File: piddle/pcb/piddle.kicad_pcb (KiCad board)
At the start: 2 copper layers, 133.5 x 118 mm, 68 parts, among them J1 Conn_01x03_Socket, J10 Conn_01x03_Socket, J11 Conn_01x02_Socket, J12 Conn_01x02_Socket, J13 Conn_01x02_Pin, J2 Conn_01x03_Socket, J3 Conn_01x03_Socket, J4 Conn_01x03_Socket, J5 Conn_01x03_Socket, J7 Conn_01x03_Socket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

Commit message: Start 15 pin
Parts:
- removed D10, D14, D16, D18, D2, D20, D4, D6, D8: 1N4148, Diode_THT:D_DO-35_SOD27_P10.16mm_Horizontal
- moved D12 14.6 mm to (87.5, 143.6), turned to 0 degrees
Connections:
- D1 pad 1: Net-(D1-VDD) -> /4.3V
- D11 pad 1: Net-(D11-VDD) -> /4.3V
- D12 pad 1: Net-(D11-VDD) -> /4.3V
- D13 pad 1: Net-(D13-VDD) -> /4.3V
- D15 pad 1: Net-(D15-VDD) -> /4.3V
- D17 pad 1: Net-(D17-VDD) -> /4.3V
- D19 pad 1: Net-(D19-VDD) -> /4.3V
- D3 pad 1: Net-(D3-VDD) -> /4.3V
- D5 pad 1: Net-(D5-VDD) -> /4.3V
- D7 pad 1: Net-(D7-VDD) -> /4.3V
- D9 pad 1: Net-(D10-K) -> /4.3V
- J7 pad 2: Net-(D13-DOUT) -> Net-(D13-DIN)
- R7 pad 1: Net-(D13-DIN) -> Net-(D13-DOUT)
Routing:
- net +5V: track 282.5 -> 72.3 mm
- net +3.3V: track 42.2 -> 14.5 mm
- net Net-(D13-VDD): track 15.2 -> 0.00 mm
- net Net-(D10-K): track 14.2 -> 0.00 mm
- net Net-(D5-VDD): track 11.5 -> 0.00 mm
- net Net-(D17-VDD): track 11.3 -> 0.00 mm
- net Net-(D19-VDD): track 11.2 -> 0.00 mm
- net Net-(D1-VDD): track 11.0 -> 0.00 mm
- net Net-(D15-VDD): track 10.4 -> 0.00 mm
- net Net-(D11-VDD): track 10.0 -> 0.00 mm
- net Net-(D7-VDD): track 9.78 -> 0.00 mm
- net Net-(D3-VDD): track 9.72 -> 0.00 mm
- net /4.3V: track 0.00 -> 1.70 mm
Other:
- board size 133.5 x 118 mm -> 198.9 x 197.8 mm

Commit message: Add mounting holes
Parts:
- added REF**: MountingHole_3.2mm_M3, MountingHole:MountingHole_3.2mm_M3, F.Cu at (74.2, 163.8)
- added REF**: MountingHole_3.2mm_M3, MountingHole:MountingHole_3.2mm_M3, F.Cu at (64.5, 71.6)
- added REF**: MountingHole_3.2mm_M3, MountingHole:MountingHole_3.2mm_M3, F.Cu at (102.5, 188.3)
- added REF**: MountingHole_3.2mm_M3, MountingHole:MountingHole_3.2mm_M3, F.Cu at (189.7, 188.3)
- added REF**: MountingHole_3.2mm_M3, MountingHole:MountingHole_3.2mm_M3, F.Cu at (229.0, 144.8)
- added REF**: MountingHole_3.2mm_M3, MountingHole:MountingHole_3.2mm_M3, F.Cu at (233.8, 129.8)
- added REF**: MountingHole_3.2mm_M3, MountingHole:MountingHole_3.2mm_M3, F.Cu at (227.7, 71.6)
- added REF**: MountingHole_3.2mm_M3, MountingHole:MountingHole_3.2mm_M3, F.Cu at (57.8, 92.4)
- added REF**: MountingHole_3.2mm_M3, MountingHole:MountingHole_3.2mm_M3, F.Cu at (138.3, 199.3)
- added REF**: MountingHole_3.2mm_M3, MountingHole:MountingHole_3.2mm_M3, F.Cu at (234.5, 92.4)
- moved REF** 180.1 mm to (219.8, 58.0)
- moved REF** 168.0 mm to (205.2, 41.7)
- moved REF** 164.9 mm to (192.5, 32.5)
- moved REF** 123.5 mm to (207.5, 175.4)
- moved REF** 121.4 mm to (218.0, 163.8)
- moved REF** 113.3 mm to (236.1, 108.0)
- moved REF** 108.0 mm to (87.1, 41.7)
- moved REF** 106.3 mm to (84.7, 175.4)
- moved REF** 98.7 mm to (119.8, 23.5)
- moved REF** 98.1 mm to (56.1, 108.0)
- moved REF** 92.0 mm to (63.3, 144.8)
- moved REF** 90.4 mm to (58.4, 129.8)
- moved REF** 88.1 mm to (172.4, 23.5)
- moved REF** 84.7 mm to (135.1, 20.3)
- moved REF** 70.7 mm to (154.0, 199.3)
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
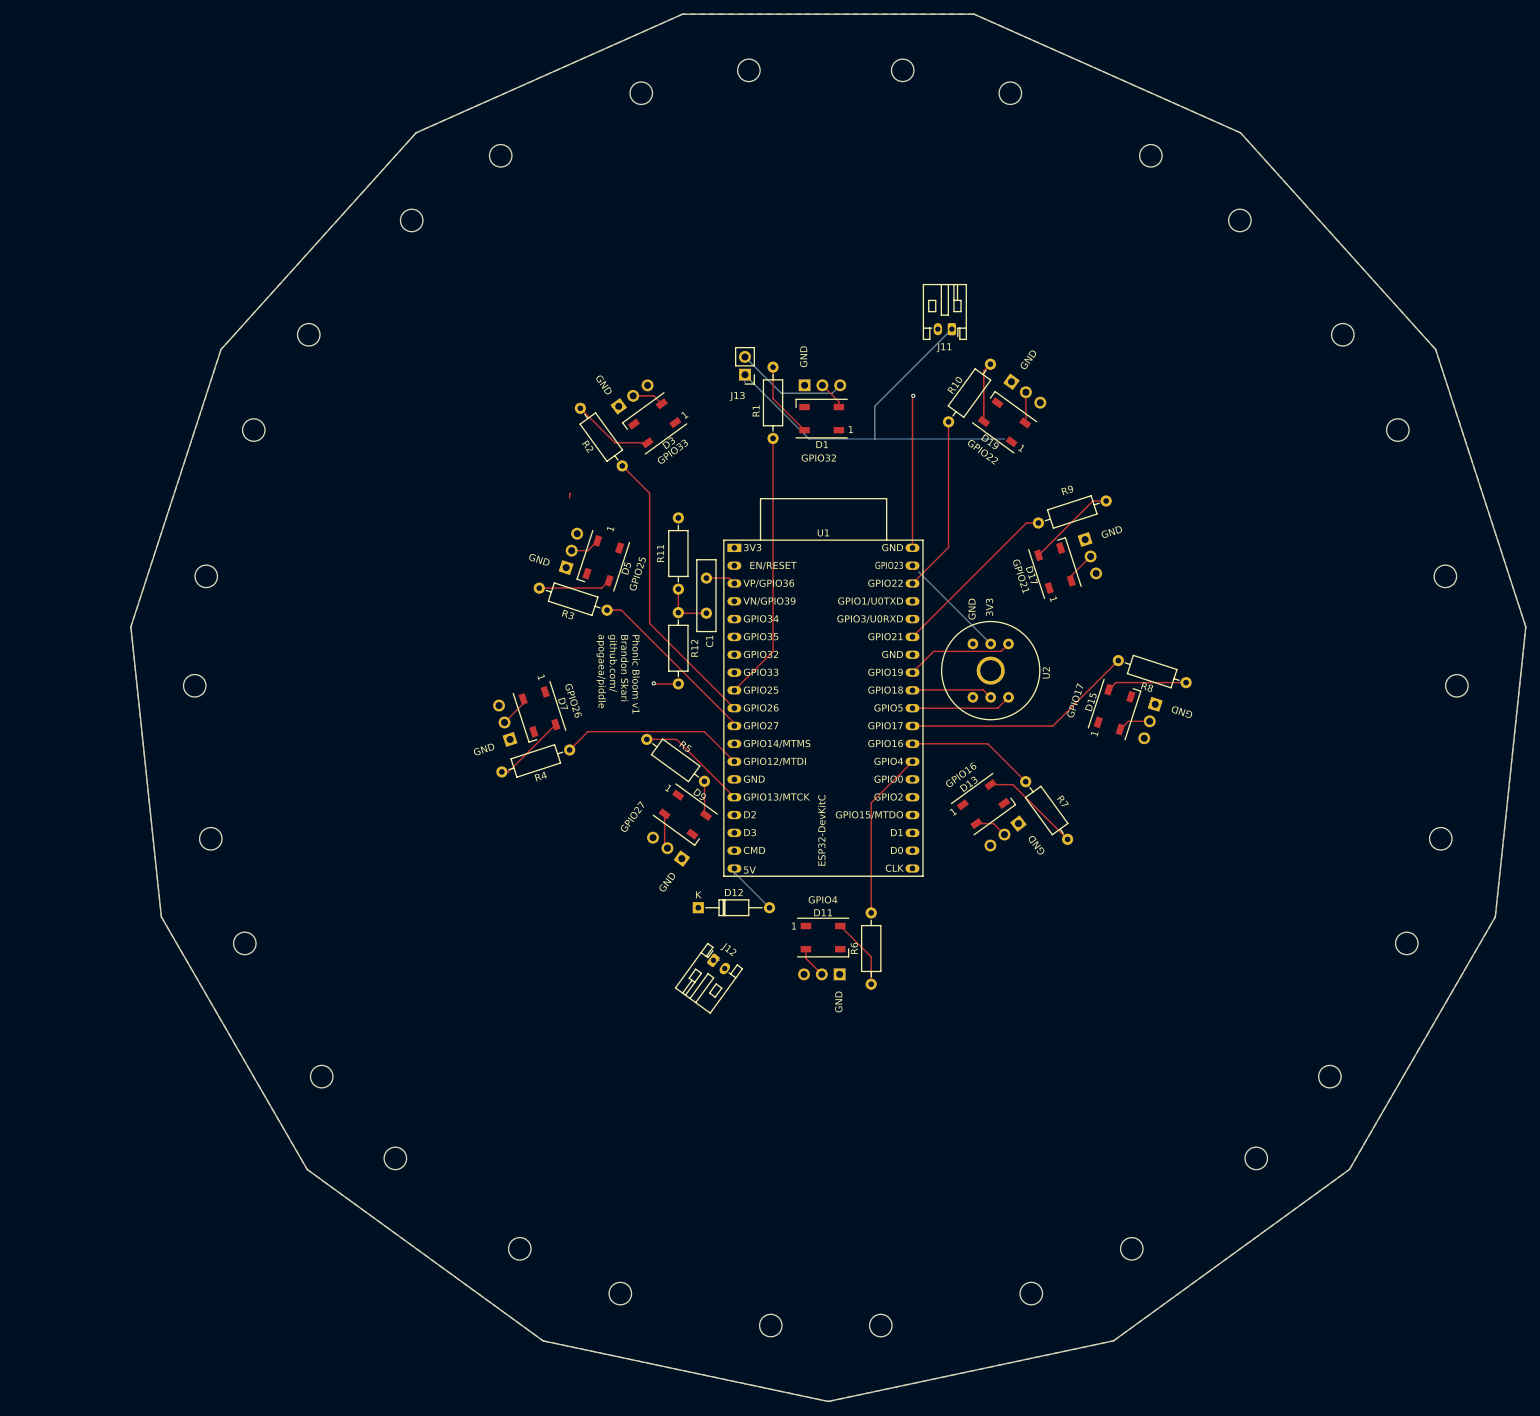
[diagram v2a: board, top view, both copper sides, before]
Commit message: Arrange components for 15-strip board
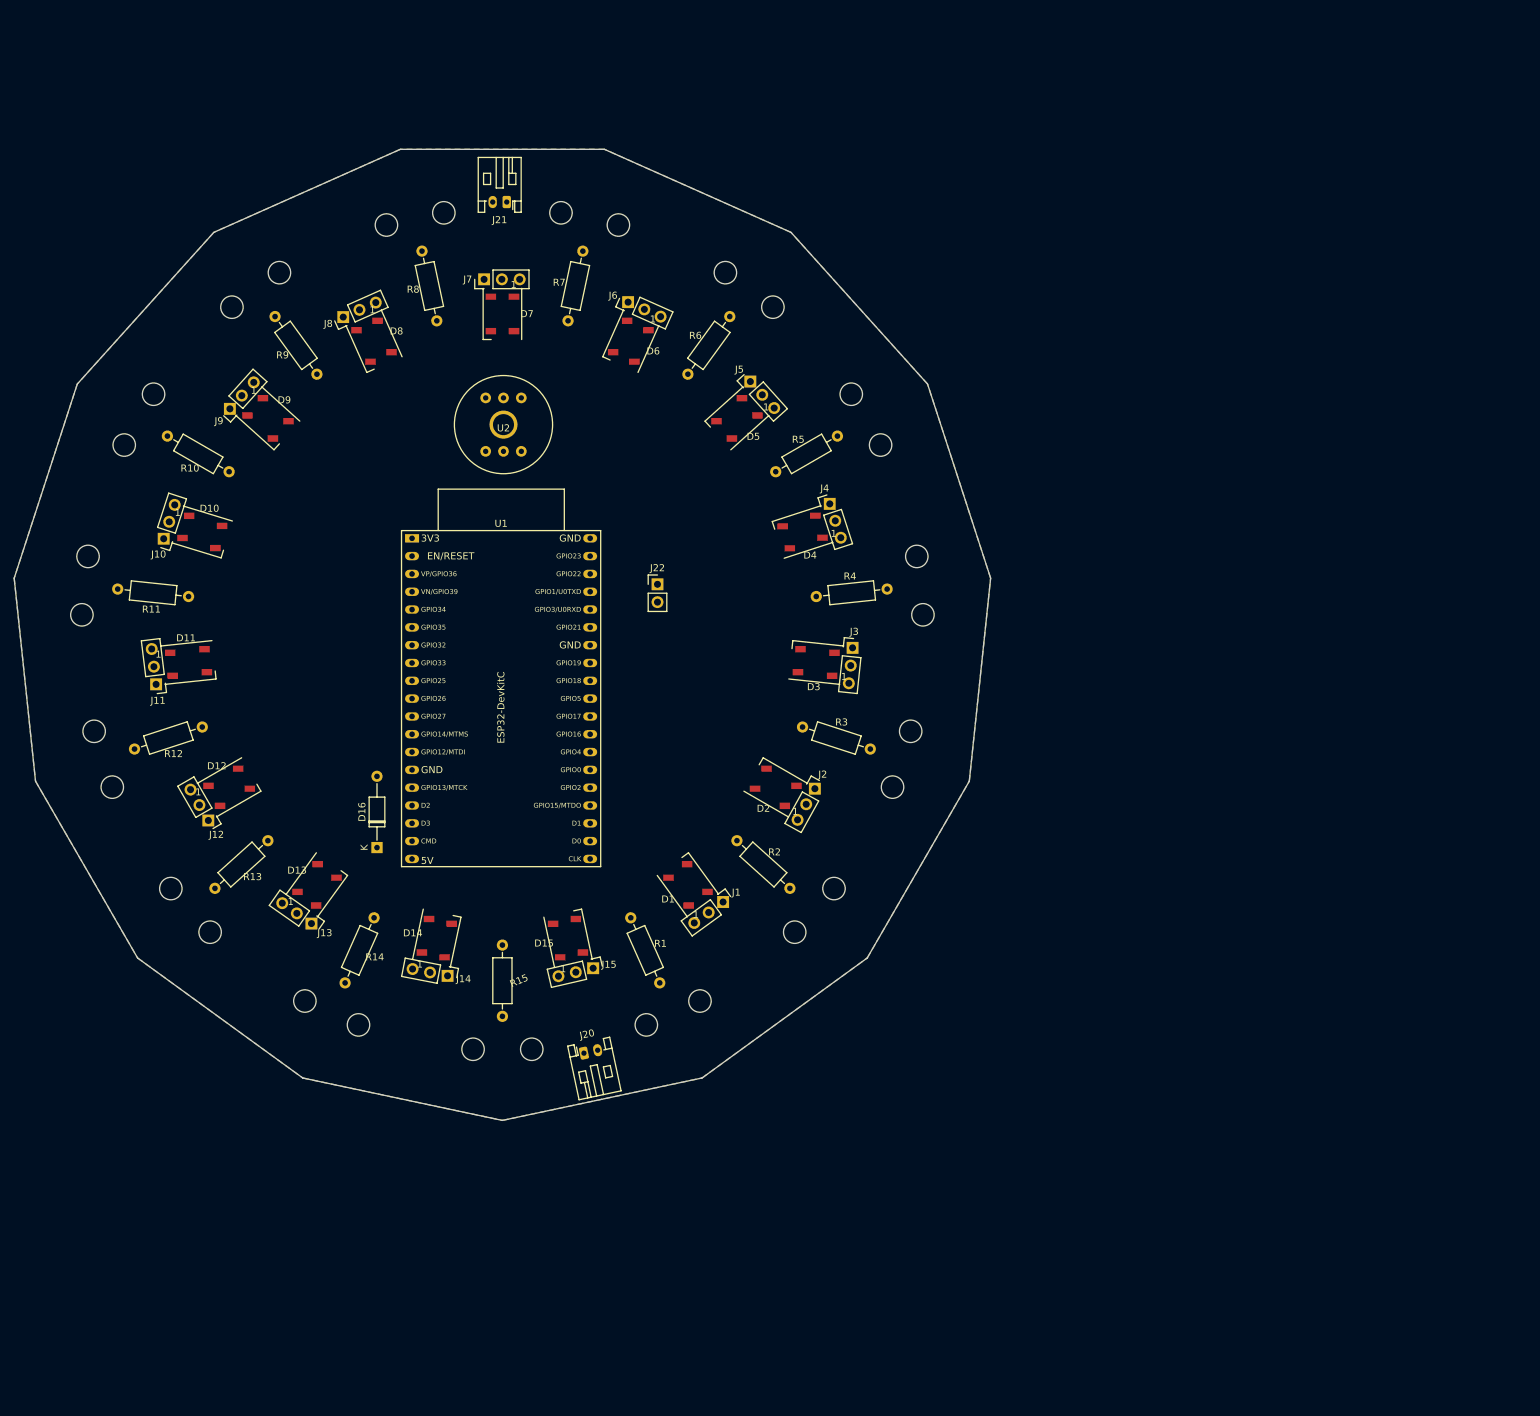
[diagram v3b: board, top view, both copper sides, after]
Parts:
- removed C1: 0.1uF, Capacitor_THT:C_Disc_D10.0mm_W2.5mm_P5.00mm
- removed D17, D19: WS2812B, LED_SMD:LED_WS2812B_PLCC4_5.0x5.0mm_P3.2mm
- removed locked: Conn_01x03_Socket, Connector_PinHeader_2.54mm:PinHeader_1x03_P2.54mm_Vertical
- added D10: WS2812B, LED_SMD:LED_WS2812B_PLCC4_5.0x5.0mm_P3.2mm, F.Cu at (57.2, 86.1)
- added D14: WS2812B, LED_SMD:LED_WS2812B_PLCC4_5.0x5.0mm_P3.2mm, F.Cu at (90.6, 144.0)
- added D16: 1N4148, Diode_THT:D_DO-35_SOD27_P10.16mm_Horizontal, F.Cu at (82.1, 131.1)
- added D2: WS2812B, LED_SMD:LED_WS2812B_PLCC4_5.0x5.0mm_P3.2mm, F.Cu at (139.0, 122.5)
- added D4: WS2812B, LED_SMD:LED_WS2812B_PLCC4_5.0x5.0mm_P3.2mm, F.Cu at (142.8, 86.1)
- added D6: WS2812B, LED_SMD:LED_WS2812B_PLCC4_5.0x5.0mm_P3.2mm, F.Cu at (118.3, 58.9)
- added D8: WS2812B, LED_SMD:LED_WS2812B_PLCC4_5.0x5.0mm_P3.2mm, F.Cu at (81.7, 58.9)
- added J14: Conn_01x03_Socket, Connector_PinHeader_2.54mm:PinHeader_1x03_P2.54mm_Vertical, F.Cu at (92.2, 149.4)
- added J15: Conn_01x03_Socket, Connector_PinHeader_2.54mm:PinHeader_1x03_P2.54mm_Vertical, F.Cu at (112.9, 148.3)
- added J20: Conn_01x02_Socket, Connector_JST:JST_PH_S2B-PH-K_1x02_P2.00mm_Horizontal, F.Cu at (111.6, 160.4)
- added J21: Conn_01x02_Socket, Connector_JST:JST_PH_S2B-PH-K_1x02_P2.00mm_Horizontal, F.Cu at (100.6, 39.0)
- added J22: Conn_01x02_Pin, Connector_PinHeader_2.54mm:PinHeader_1x02_P2.54mm_Vertical, F.Cu at (122.1, 93.6)
- added J6: Conn_01x03_Socket, Connector_PinHeader_2.54mm:PinHeader_1x03_P2.54mm_Vertical, F.Cu at (117.9, 53.3)
- added R13: 400, Resistor_THT:R_Axial_DIN0207_L6.3mm_D2.5mm_P10.16mm_Horizontal, F.Cu at (66.6, 130.1)
- added R14: 400, Resistor_THT:R_Axial_DIN0207_L6.3mm_D2.5mm_P10.16mm_Horizontal, F.Cu at (81.7, 141.1)
- added R15: 400, Resistor_THT:R_Axial_DIN0207_L6.3mm_D2.5mm_P10.16mm_Horizontal, F.Cu at (100.0, 145.0)
- D12: value 1N4148 -> WS2812B; footprint Diode_THT:D_DO-35_SOD27_P10.16mm_Horizontal -> LED_SMD:LED_WS2812B_PLCC4_5.0x5.0mm_P3.2mm
- J1, J10, J2, J3, J4, J5, J7, J8, J9: moved to F.Cu
- J11, J12: value Conn_01x02_Socket -> Conn_01x03_Socket; footprint Connector_JST:JST_PH_S2B-PH-K_1x02_P2.00mm_Horizontal -> Connector_PinHeader_2.54mm:PinHeader_1x03_P2.54mm_Vertical
- J13: value Conn_01x02_Pin -> Conn_01x03_Socket; footprint Connector_PinHeader_2.54mm:PinHeader_1x02_P2.54mm_Vertical -> Connector_PinHeader_2.54mm:PinHeader_1x03_P2.54mm_Vertical
- R11, R12: value 10000 -> 400
- moved REF** 159.1 mm to (83.5, 42.3)
- moved REF** 158.5 mm to (61.4, 54.0)
- moved REF** 154.0 mm to (108.4, 40.6)
- moved REF** 152.1 mm to (46.1, 73.7)
- moved REF** 143.4 mm to (131.8, 49.1)
- moved REF** 140.5 mm to (40.0, 97.9)
- moved REF** 139.5 mm to (91.6, 40.6)
- moved REF** 137.2 mm to (68.2, 49.1)
- moved REF** 136.4 mm to (116.5, 42.3)
- moved REF** 129.5 mm to (50.3, 66.4)
- moved J8 128.3 mm to (77.3, 55.4), turned to 114 degrees
- moved REF** 128.3 mm to (149.7, 66.4)
- moved REF** 128.1 mm to (138.6, 54.0)
- moved REF** 124.4 mm to (44.4, 122.5)
- moved J11 124.3 mm to (50.6, 107.8), turned to -173 degrees
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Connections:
- D12 pad 2: +5V -> Net-(D12-DOUT)
- J1 pad 3: Net-(J1-Pin_3) -> unconnected-(J1-Pin_3-Pad3)
- J11 pad 1: +5V -> GND
- J11 pad 2: GND -> Net-(D11-DOUT)
- J12 pad 1: +5V -> GND
- J12 pad 2: GND -> Net-(D12-DOUT)
- J13 pad 1: +5V -> GND
- J13 pad 2: Net-(J1-Pin_3) -> Net-(D13-DOUT)
- J2 pad 2: Net-(D3-DOUT) -> Net-(D2-DOUT)
- J3 pad 2: Net-(D5-DOUT) -> Net-(D3-DOUT)
- J4 pad 2: Net-(D7-DOUT) -> Net-(D4-DIN)
- J5 pad 2: Net-(D9-DOUT) -> Net-(D5-DOUT)
- J7 pad 2: Net-(D13-DIN) -> Net-(D7-DOUT)
- J8 pad 2: Net-(D15-DOUT) -> Net-(D8-DOUT)
- J9 pad 2: Net-(D17-DOUT) -> Net-(D9-DOUT)
- R1 pad 1: /GPIO25 -> /GPIO15
- R10 pad 1: Net-(D19-DIN) -> /GPIO33
- R10 pad 2: /GPIO22 -> Net-(D10-DIN)
- R11 pad 1: +5V -> /GPIO25
- R11 pad 2: Net-(C1-Pad2) -> Net-(D11-DIN)
- R12 pad 1: Net-(C1-Pad2) -> /GPIO26
- R12 pad 2: GND -> Net-(D12-DIN)
- R2 pad 1: /GPIO26 -> /GPIO4
- R2 pad 2: Net-(D3-DIN) -> Net-(D2-DIN)
- R3 pad 1: /GPIO27 -> /GPIO16
- R3 pad 2: Net-(D5-DIN) -> Net-(D3-DIN)
- R4 pad 1: /GPIO12 -> /GPIO17
- R4 pad 2: Net-(D7-DIN) -> Net-(D4-DOUT)
- R5 pad 1: /GPIO13 -> /GPIO5
- R5 pad 2: Net-(D9-DIN) -> Net-(D5-DIN)
- R6 pad 1: Net-(D11-DIN) -> /GPIO18
- R6 pad 2: /GPIO4 -> Net-(D6-DOUT)
- R7 pad 1: Net-(D13-DOUT) -> /GPIO19
- R7 pad 2: /GPIO16 -> Net-(D7-DIN)
- R8 pad 1: Net-(D15-DIN) -> /GPIO21
- R8 pad 2: /GPIO17 -> Net-(D8-DIN)
- R9 pad 1: Net-(D17-DIN) -> /GPIO32
- R9 pad 2: /GPIO21 -> Net-(D9-DIN)
- U2 pad 3: /GPIO19 -> /GPIO36
- U2 pad 5: /GPIO18 -> /GPIO23
- U2 pad 6: /GPIO5 -> /GPIO22
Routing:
- net +5V: track 72.3 -> 0.00 mm
- net /GPIO26: track 41.2 -> 0.00 mm
- net /GPIO25: track 38.2 -> 0.00 mm
- net /GPIO17: track 33.2 -> 0.00 mm
- net /GPIO12: track 26.3 -> 0.00 mm
- net GND: track 25.3 -> 0.00 mm, vias 2 -> 0
- net /GPIO27: track 25.2 -> 0.00 mm
- net /GPIO22: track 25.2 -> 0.00 mm
- net /GPIO21: track 24.7 -> 0.00 mm
- net /GPIO4: track 24.0 -> 0.00 mm
- net /GPIO16: track 18.4 -> 0.00 mm
- net Net-(J1-Pin_3): track 16.2 -> 0.00 mm
- net /GPIO13: track 15.9 -> 0.00 mm
- net /GPIO19: track 15.4 -> 0.00 mm
- net +3.3V: track 14.5 -> 0.00 mm
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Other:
- board size 198.9 x 197.8 mm -> 139.2 x 138.5 mm
- board text removed: "3V3"
- board text removed: "GND"
- board text removed: "GPIO16"
- board text removed: "GPIO17"
- board text removed: "GPIO21"
- board text removed: "GPIO22"
- board text removed: "GPIO25"
- board text removed: "GPIO26"
- board text removed: "GPIO27"
- board text removed: "GPIO32"
- board text removed: "GPIO33"
- board text removed: "GPIO4"
- board text removed: "Phonic Bloom v1 Brandon Skari github.com/ apogaea/piddle"
